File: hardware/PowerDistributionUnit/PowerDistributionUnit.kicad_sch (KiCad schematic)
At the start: 42 parts, among them J0 Conn_01x02, J1 Conn_01x02, J10 Conn_01x02, J11 Conn_01x02, J12 Conn_01x02, J13 Conn_01x02, J14 Conn_01x04, J15 Conn_01x04, J16 Conn_01x02, J17 Conn_01x02, J2 Conn_01x02, J3 Conn_01x02, J4 Conn_01x02, J5 Conn_01x02, J6 Conn_01x02, J7 Conn_01x02, J8 Conn_01x02, J9 Conn_01x02, Q17 SQJ141ELP, U34 PeripheralSOM

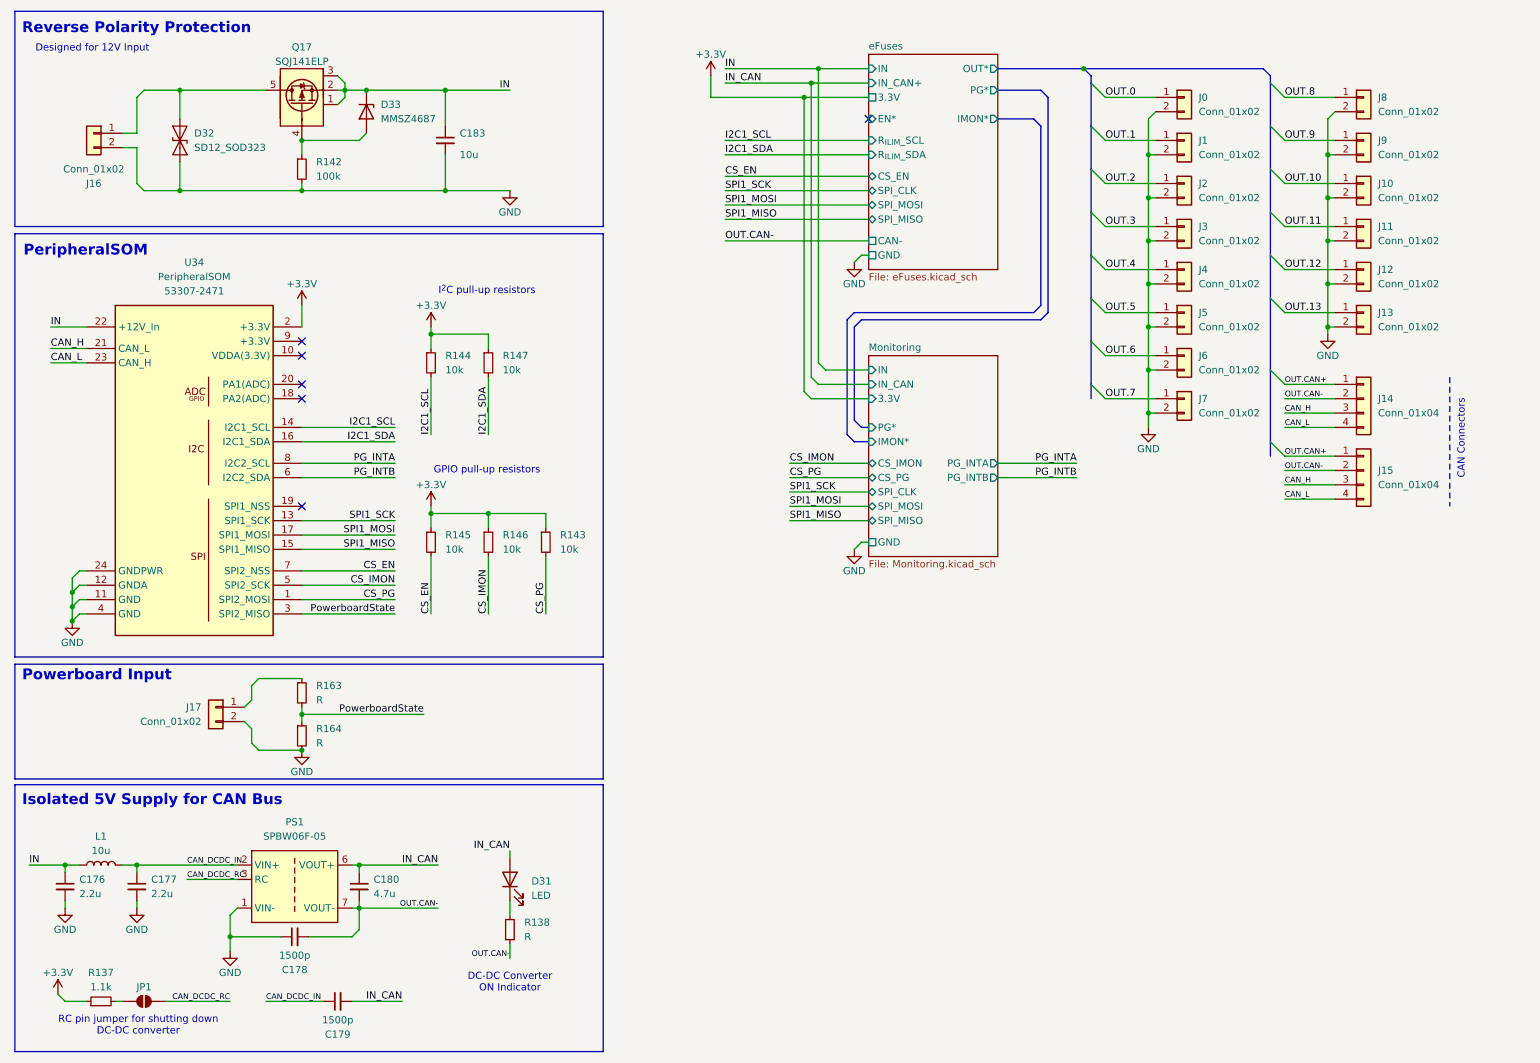
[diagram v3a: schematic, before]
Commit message: Began eFuse test schematic
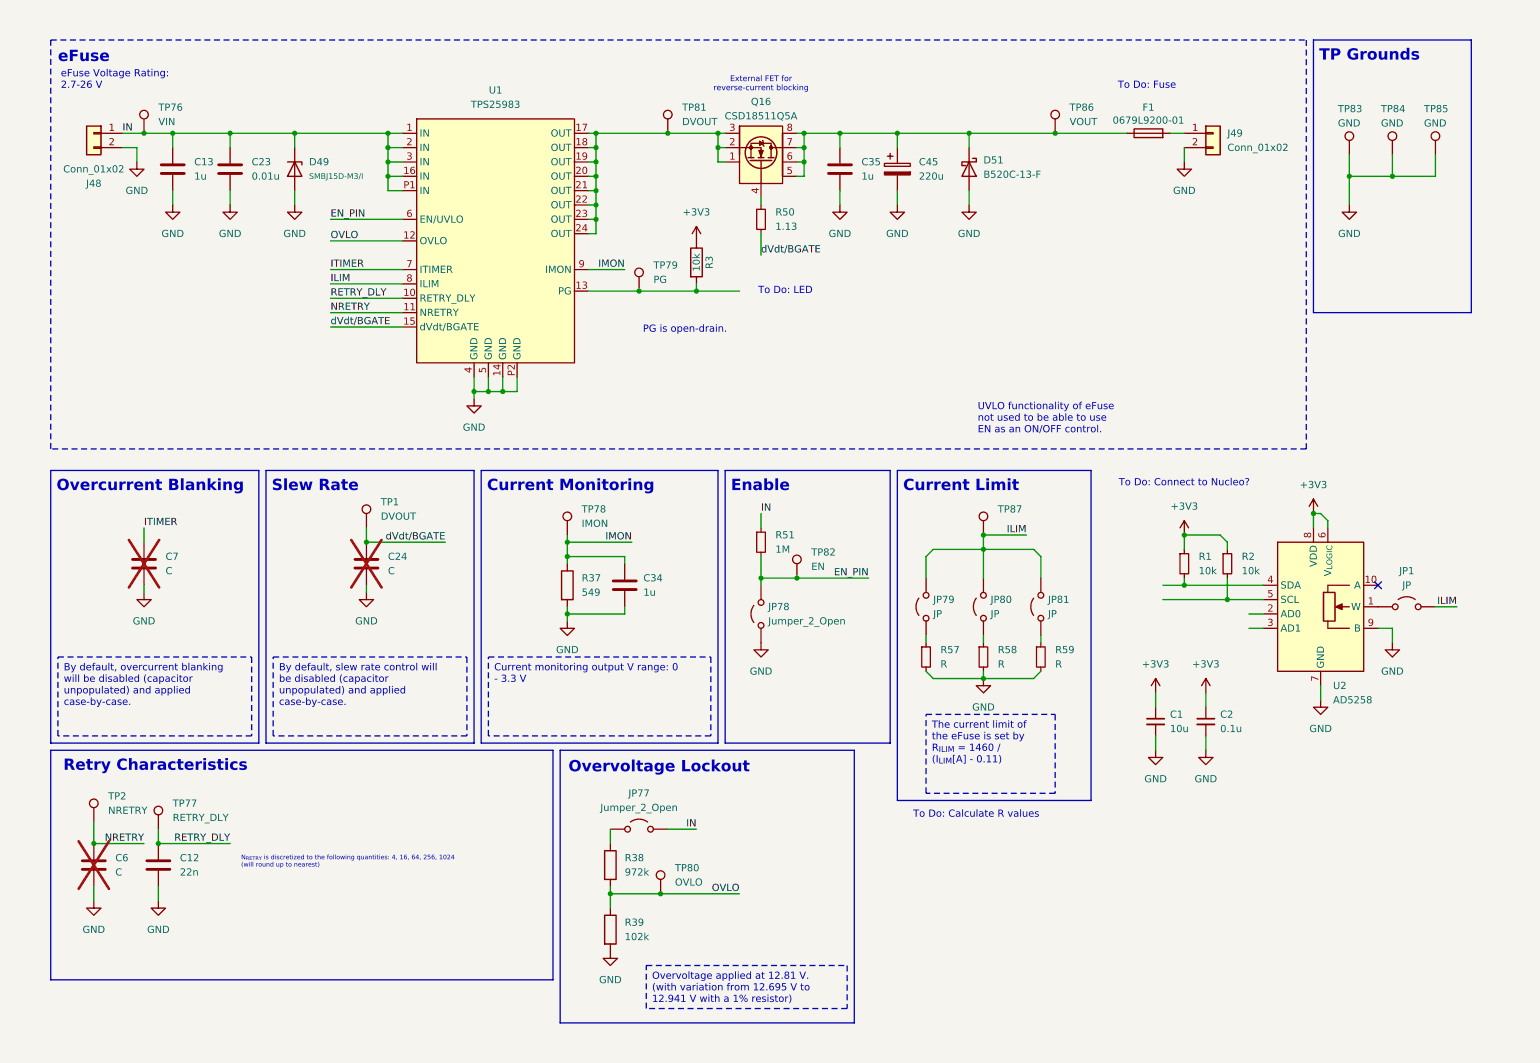
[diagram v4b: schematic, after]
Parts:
- removed C176, C177: 2.2u, symbol Device:C_Small
- removed C178, C179: 1500p, symbol Device:C_Small
- removed C180: 4.7u, symbol Device:C_Small
- removed C183: 10u, symbol Device:C_Small
- removed D31: LED, symbol Device:LED
- removed D32: SD12_SOD323, Diode_SMD:D_SOD-323, symbol Diode:SD12_SOD323
- removed D33: MMSZ4687, Diode_SMD:D_SOD-123, symbol Device:D_Zener
- removed J0, J1, J10, J11, J12, J13, J16, J17, J2, J3, J4, J5, J6, J7, J8, J9: Conn_01x02, symbol Connector_Generic:Conn_01x02
- removed J14, J15: Conn_01x04, symbol Connector_Generic:Conn_01x04
- removed JP1: SolderJumper_2_Open, Jumper:SolderJumper-2_P1.3mm_Open_TrianglePad1.0x1.5mm, symbol Jumper:SolderJumper_2_Open
- removed L1: 10u, symbol Device:L
- removed PS1: SPBW06F-05, PowerDistributionUnitLib:SPBW06F-xx, symbol PowerDistributionUnitLib:SPBW06F-xx
- removed Q17: SQJ141ELP, Package_SO:PowerPAK_SO-8L_Single, symbol PowerDistributionUnitLib:SQJ141ELP
- removed R137: 1.1k, symbol Device:R_Small
- removed R138, R163, R164: R, symbol Device:R_Small
- removed R142: 100k, symbol Device:R_Small
- removed R143, R144, R145, R146, R147: 10k, symbol Device:R_Small
- removed U34: PeripheralSOM, UTSVT_Special:PeripheralSOM, symbol utsvt-misc:PeripheralSOM
- added C1: 10u, symbol Device:C_Small
- added C12: 22n, symbol Device:C
- added C13, C34, C35: 1u, symbol Device:C
- added C2: 0.1u, symbol Device:C_Small
- added C23: 0.01u, symbol Device:C
- added C24, C6, C7: C, symbol Device:C
- added C45: 220u, Capacitor_SMD:CP_Elec_10x10.5, symbol Device:C_Polarized
- added D49: SMBJ15D-M3/I, Diode_SMD:D_SMB, symbol Device:D_Zener
- added D51: B520C-13-F, Diode_SMD:D_SMC, symbol Device:D_Schottky
- added F1: 0679L9200-01, symbol Device:Fuse
- added J48, J49: Conn_01x02, symbol Connector_Generic:Conn_01x02
- added JP1, JP79, JP80, JP81: JP, symbol Jumper:Jumper_2_Open
- added JP77, JP78: Jumper_2_Open, symbol Jumper:Jumper_2_Open
- added Q16: CSD18511Q5A, Package_SON:VSONP-8-1EP_5x6_P1.27mm, symbol PowerDistributionUnitLib:CSD18511Q5A
- added R1, R2: 10k, symbol Device:R_Small
- added R3: 10k, symbol Device:R
- added R37: 549, symbol Device:R
- added R38: 972k, symbol Device:R
- added R39: 102k, symbol Device:R
- added R50: 1.13, symbol Device:R_Small
- added R51: 1M, symbol Device:R_Small
- added R57, R58, R59: R, symbol Device:R_Small
- added TP1, TP81: DVOUT, symbol Connector:TestPoint
- added TP2: NRETRY, symbol Connector:TestPoint
- added TP76: VIN, symbol Connector:TestPoint
- added TP77: RETRY_DLY, symbol Connector:TestPoint
- added TP78: IMON, symbol Connector:TestPoint
- added TP79: PG, symbol Connector:TestPoint
- added TP80: OVLO, symbol Connector:TestPoint
- added TP82: EN, symbol Connector:TestPoint
- added TP83, TP84, TP85: GND, symbol Connector:TestPoint
- added TP86: VOUT, symbol Connector:TestPoint
- added TP87: ILIM, symbol Connector:TestPoint
- added U1: TPS25983, PowerDistributionUnitLib:TPS25983, symbol PowerDistributionUnitLib:TPS25983
- added U2: AD5258, Package_SO:MSOP-10_3x3mm_P0.5mm, symbol PowerDistributionUnitLib:AD5258
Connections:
- net GND: now also C1.2, C12.2, C13.2, C2.2, C23.2, C24.2, C34.2, C35.2, C45.2, C6.2, C7.2, D49.2 (A), D51.2 (A), J48.2 (Pin_2), J49.2 (Pin_2), JP78.1 (A), R37.2, R39.2, R57.2, R58.2, R59.2, TP83.1, TP84.1, TP85.1, U1.14 (GND), U1.4 (GND), U1.5 (GND), U1.P2 (GND), U2.7 (GND), U2.9 (B)
- net IN: now also C13.1, C23.1, D49.1 (K), J48.1 (Pin_1), JP77.2 (B), R51.1, TP76.1, U1.1 (IN), U1.16 (IN), U1.2 (IN), U1.3 (IN), U1.P1 (IN)
- new net: JP1.1 (A), U2.1 (W)
- new net: C35.1, C45.1, D51.1 (K), F1.1, Q16.5, Q16.6, Q16.7, Q16.8, TP86.1
- new net: F1.2, J49.1 (Pin_1)
- new net: JP80.1 (A), R58.1
- new net: JP81.1 (A), R59.1
- new net: JP77.1 (A), R38.1
- new net: JP79.1 (A), R57.1
- new net: Q16.1, Q16.2, Q16.3, TP81.1, U1.17 (OUT), U1.18 (OUT), U1.19 (OUT), U1.20 (OUT), U1.21 (OUT), U1.22 (OUT), U1.23 (OUT), U1.24 (OUT)
- new net: R3.2, TP79.1, U1.13 (PG)
- new net: R2.2, U2.5 (SCL)
- new net: R1.2, U2.4 (SDA)
- new net: Q16.4, R50.1
- new net +3V3: C1.1, C2.1, R1.1, R2.1, R3.1, U2.6 (V_{LOGIC}), U2.8 (VDD)
- new net EN_PIN: JP78.2 (B), R51.2, TP82.1, U1.6 (EN/UVLO)
- new net ILIM: JP1.2 (B), JP79.2 (B), JP80.2 (B), JP81.2 (B), TP87.1, U1.8 (ILIM)
- new net IMON: C34.1, R37.1, TP78.1, U1.9 (IMON)
- new net ITIMER: C7.1, U1.7 (ITIMER)
- new net NRETRY: C6.1, TP2.1, U1.11 (NRETRY)
- new net OVLO: R38.2, R39.1, TP80.1, U1.12 (OVLO)
- new net RETRY_DLY: C12.1, TP77.1, U1.10 (RETRY_DLY)
- new net dVdt/BGATE: C24.1, R50.2, TP1.1, U1.15 (dVdt/BGATE)
- no-connect marks 6 -> 1
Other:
- removed sheet Monitoring
- removed sheet eFuses
- note added: "Current Limit"
- note added: "Current Monitoring"
- note added: "Enable"
- note added: "Overcurrent Blanking"
- note added: "Overvoltage Lockout"
- note added: "PG is open-drain."
- note added: "Retry Characteristics"
- note added: "Slew Rate"
- note added: "TP Grounds"
- note added: "To Do: Calculate R values"
- note added: "To Do: Connect to Nucleo?"
- note added: "To Do: Fuse"
- note added: "To Do: LED"
- note added: "UVLO functionality of eFuse not used to be able to use EN as an ON/OFF control."
- note added: "eFuse"
- note added: "eFuse Voltage Rating: 2.7-26 V"
- note removed: "CAN Connectors"
- note removed: "DC-DC Converter ON Indicator"
- note removed: "Designed for 12V Input"
- note removed: "GPIO pull-up resistors"
- note removed: "I^{2}C pull-up resistors"
- note removed: "Isolated 5V Supply for CAN Bus"
- note removed: "PeripheralSOM"
- note removed: "Powerboard Input"
- note removed: "RC pin jumper for shutting down DC-DC converter"
- note removed: "Reverse Polarity Protection"

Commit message: changed connectors to banana connectors
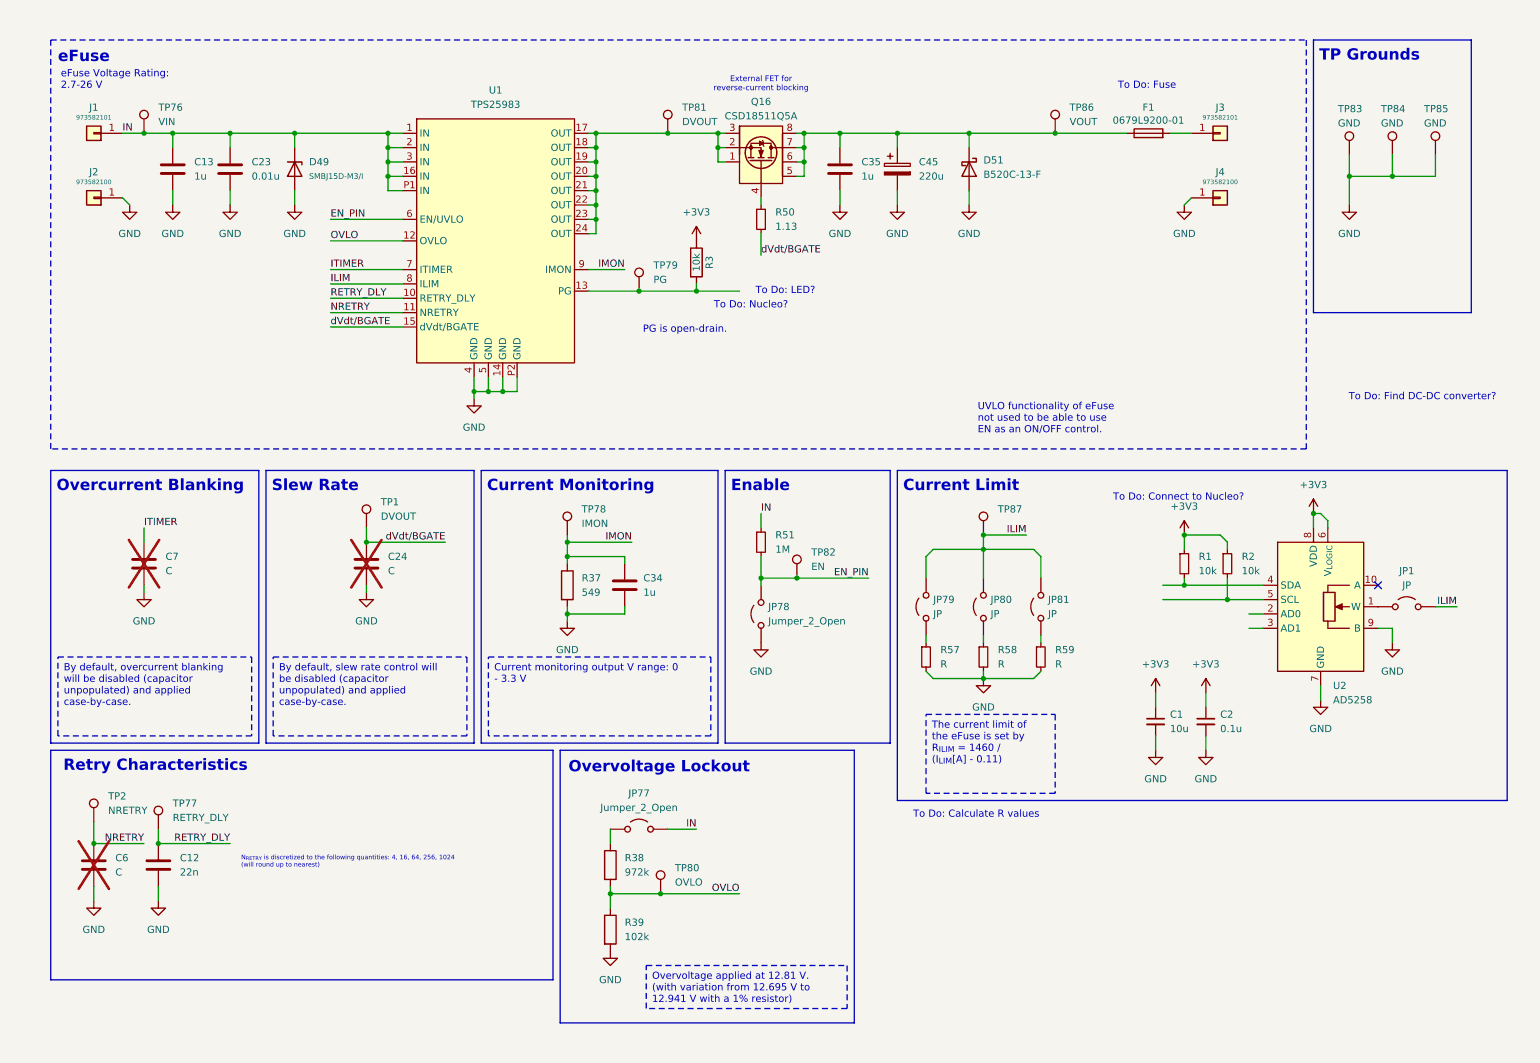
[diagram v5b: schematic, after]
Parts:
- removed J48, J49: Conn_01x02, symbol Connector_Generic:Conn_01x02
- added J1, J3: 973582101, PowerDistributionUnitLib:973582101, symbol Connector_Generic:Conn_01x01
- added J2, J4: 973582100, PowerDistributionUnitLib:973582100, symbol Connector_Generic:Conn_01x01
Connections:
- net GND: now also J2.1 (Pin_1), J4.1 (Pin_1)
- net IN: now also J1.1 (Pin_1)
- net at F1.2: now also J3.1 (Pin_1)
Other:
- note added: "To Do: Find DC-DC converter?"
- note added: "To Do: LED?"
- note added: "To Do: Nucleo?"
- note removed: "To Do: LED"

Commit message: schematic work
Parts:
- removed C12: 22n, symbol Device:C
- removed C24, C6, C7: C, symbol Device:C
- removed JP78: Jumper_2_Open, symbol Jumper:Jumper_2_Open
- removed R51: 1M, symbol Device:R_Small
- removed TP83, TP84, TP85: GND, symbol Connector:TestPoint
- added C10: 0.47n, symbol Device:C_Small
- added C11, C16: 4.7n, symbol Device:C_Small
- added C12, C6: 1u, symbol Device:C_Small
- added C14: 47n, symbol Device:C_Small
- added C15: 3n, symbol Device:C_Small
- added C17: 10n, symbol Device:C_Small
- added C3: 220n, symbol Device:C_Small
- added C4, C7: 22n, symbol Device:C_Small
- added C5, C8: 2.2n, symbol Device:C_Small
- added C9: 220p, symbol Device:C_Small
- added D1: 587-1016-247F, PowerDistributionUnitLib:587-1016-247F, symbol PowerDistributionUnitLib:587-1016-247F
- added JP10, JP19: JP, symbol Jumper:Jumper_2_Small_Open
- added JP11: 200 us, symbol Jumper:Jumper_2_Small_Open
- added JP12: 2 ms, symbol Jumper:Jumper_2_Small_Open
- added JP13: 20 ms, symbol Jumper:Jumper_2_Small_Open
- added JP14: 1.5 V/ms, symbol Jumper:Jumper_2_Small_Open
- added JP15: 1 V/ms, symbol Jumper:Jumper_2_Small_Open
- added JP16: 0.5 V/ms, symbol Jumper:Jumper_2_Small_Open
- added JP17: Latching, symbol Jumper:Jumper_2_Small_Open
- added JP18: Inf, symbol Jumper:Jumper_2_Small_Open
- added JP2, JP3: Jumper_2_Small_Open, symbol Jumper:Jumper_2_Small_Open
- added JP4: 16 (915 ms), symbol Jumper:Jumper_2_Small_Open
- added JP5: 16 (91.7 ms), symbol Jumper:Jumper_2_Small_Open
- added JP6: 16 (9.3 ms), symbol Jumper:Jumper_2_Small_Open
- added JP7: 915 ms, symbol Jumper:Jumper_2_Small_Open
- added JP8: 91.7 ms, symbol Jumper:Jumper_2_Small_Open
- added JP9: 9.3 ms, symbol Jumper:Jumper_2_Small_Open
- added R4, R5, R9: 1k, symbol Device:R_Small
- added R6: 1k, symbol Device:R
- added R7: 13k, symbol Device:R
- added R8: 2.49k, symbol Device:R
- added SW1: SW_Push, Button_Switch_SMD:SW_SPST_PTS645, symbol Switch:SW_Push
- added TP10, TP11, TP12, TP13, TP9: VIN, symbol Connector:TestPoint
- added TP3: ITIMER, symbol Connector:TestPoint
- added TP4: 3.3V, symbol Connector:TestPoint
- added TP5, TP6, TP7, TP8: GND, symbol Connector:TestPoint
- added U3: NUCLEO_LK43C, symbol PowerDistributionUnitLib:NUCLEO_L43KC
- JP1: symbol Jumper:Jumper_2_Open -> Jumper:Jumper_2_Small_Open
- JP77: value Jumper_2_Open -> OVLO_DISABLE; symbol Jumper:Jumper_2_Open -> Jumper:Jumper_2_Small_Open
- JP79: value JP -> ~2A; symbol Jumper:Jumper_2_Open -> Jumper:Jumper_2_Small_Open
- JP80: value JP -> ~5A; symbol Jumper:Jumper_2_Open -> Jumper:Jumper_2_Small_Open
- JP81: value JP -> ~12A; symbol Jumper:Jumper_2_Open -> Jumper:Jumper_2_Small_Open
- R57: value R -> 768
- R58: value R -> 294
- R59: value R -> 121
- TP81: value DVOUT -> EFET_S
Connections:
- net +3V3: now also C12.1, C6.1, D1.4 (VCC), JP10.2 (B), JP2.2 (B), JP3.2 (B), R9.1, TP4.1, U3.CN4_14 (+3V3)
- net EN_PIN: now also JP10.1 (A), JP19.2 (B), R6.1
- net GND: now also C10.2, C11.2, C12.2, C14.2, C15.2, C16.2, C17.2, C3.2, C4.2, C5.2, C6.2, C7.2, C8.2, C9.2, D1.1 (GND), JP17.1 (A), JP18.1 (A), R4.2, R5.2, R6.2, R8.2, SW1.2, TP5.1, TP6.1, TP7.1, TP8.1, U3.CN3_4 (GND), U3.CN4_2 (GND)
- net IMON: now also U3.CN4_9 (PA4)
- net IN: now also R7.1
- net ITIMER: now also JP11.2 (B), JP12.2 (B), JP13.2 (B), TP3.1
- net NRETRY: now also JP18.2 (B), JP4.2 (B), JP5.2 (B), JP6.2 (B)
- net RETRY_DLY: now also JP17.2 (B), JP7.2 (B), JP8.2 (B), JP9.2 (B)
- net dVdt/BGATE: now also JP14.2 (B), JP15.2 (B), JP16.2 (B)
- net EFUSE_OUT: now reaches C35.1, C45.1, D51.1 (K), F1.1, Q16.5, Q16.6, Q16.7, Q16.8, TP86.1
- net EFET_S: now reaches Q16.1, Q16.2, Q16.3, TP81.1, U1.17 (OUT), U1.18 (OUT), U1.19 (OUT), U1.20 (OUT), U1.21 (OUT), U1.22 (OUT), U1.23 (OUT), U1.24 (OUT)
- net PG: now reaches R3.2, TP79.1, U1.13 (PG)
- net PG: now also U3.CN4_5 (PA2)
- net ILIM_SCL: now reaches R2.2, U2.5 (SCL)
- net ILIM_SCL: now also TP10.1, U3.CN4_7 (PA6)
- net ILIM_AD0: now reaches U2.2 (AD0)
- net ILIM_AD0: now also JP2.1 (A), R4.1
- net ILIM_AD1: now reaches U2.3 (AD1)
- net ILIM_AD1: now also JP3.1 (A), R5.1
- net ILIM_SDA: now reaches R1.2, U2.4 (SDA)
- net ILIM_SDA: now also TP11.1, U3.CN4_8 (PA5)
- new net: C4.1, JP5.1 (A)
- new net: C17.1, JP16.1 (A)
- new net: C15.1, JP14.1 (A)
- new net: C9.1, JP9.1 (A)
- new net: C5.1, JP6.1 (A)
- new net: C3.1, JP4.1 (A)
- new net: C10.1, JP11.1 (A)
- new net: C16.1, JP15.1 (A)
- new net: C11.1, JP12.1 (A)
- new net: C8.1, JP8.1 (A)
- new net: C7.1, JP7.1 (A)
- new net: C14.1, JP13.1 (A)
- new net: JP19.1 (A), U3.CN4_10 (PA3)
- new net IND_BTN: R9.2, SW1.1, U3.CN3_12 (PA8)
- new net IN_SENSE: R7.2, R8.1, TP9.1, U3.CN4_6 (PA7)
- new net LED_CK: D1.5 (CKI), TP12.1, U3.CN4_12 (PA0)
- new net LED_SD: D1.6 (SDI), TP13.1, U3.CN4_11 (PA1)
- no-connect marks 1 -> 21
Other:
- note added: "# OF RETRIES"
- note added: "(4 - OPEN)"
- note added: "(Instantaneous - OPEN)"
- note added: "(Min delay - OPEN)"
- note added: "(OFF - OPEN)"
- note added: "Bypass Capacitors"
- note added: "I2C Address Selection"
- note added: "Indicator"
- note added: "Input Sensing"
- note added: "Nucleo"
- note added: "OVLO"
- note added: "PRESET RESISTANCES"
- note added: "PROGRAMMABLE DIGITAL POT"
- note added: "RETRY DELAY"
- note added: "Test Points"
- note removed: "Overvoltage Lockout"
- note removed: "TP Grounds"
- note removed: "To Do: Calculate R values"
- note removed: "To Do: Connect to Nucleo?"
- note removed: "To Do: Find DC-DC converter?"
- note removed: "To Do: Fuse"
- note removed: "To Do: LED?"
- note removed: "To Do: Nucleo?"
- company: (none) -> Longhorn Racing: Solar
- title: (none) -> eFuse Test Board
- moved on the sheet: C1, C13, C2, C23, C34, C35, C45, D49, D51, F1, J1, J2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
